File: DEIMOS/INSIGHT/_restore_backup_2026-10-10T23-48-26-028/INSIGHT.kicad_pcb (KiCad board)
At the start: 4 copper layers, 69.9 x 26 mm, 79 parts, among them J1 Batt, J3 USB_C_Receptacle_USB2.0_16P, J4 Boot, J5 GND, J8 5V, SW3 SW_SPDT, U1 LSM6DS3, U11 MPM3610GQV-Z, U2 MPL3115A2, U3 W25Q128JVSIQ, U5 RP2040, U6 Adafruit GPS, U7 MPM3610GQV-Z, Y1 ABM8-272-T3

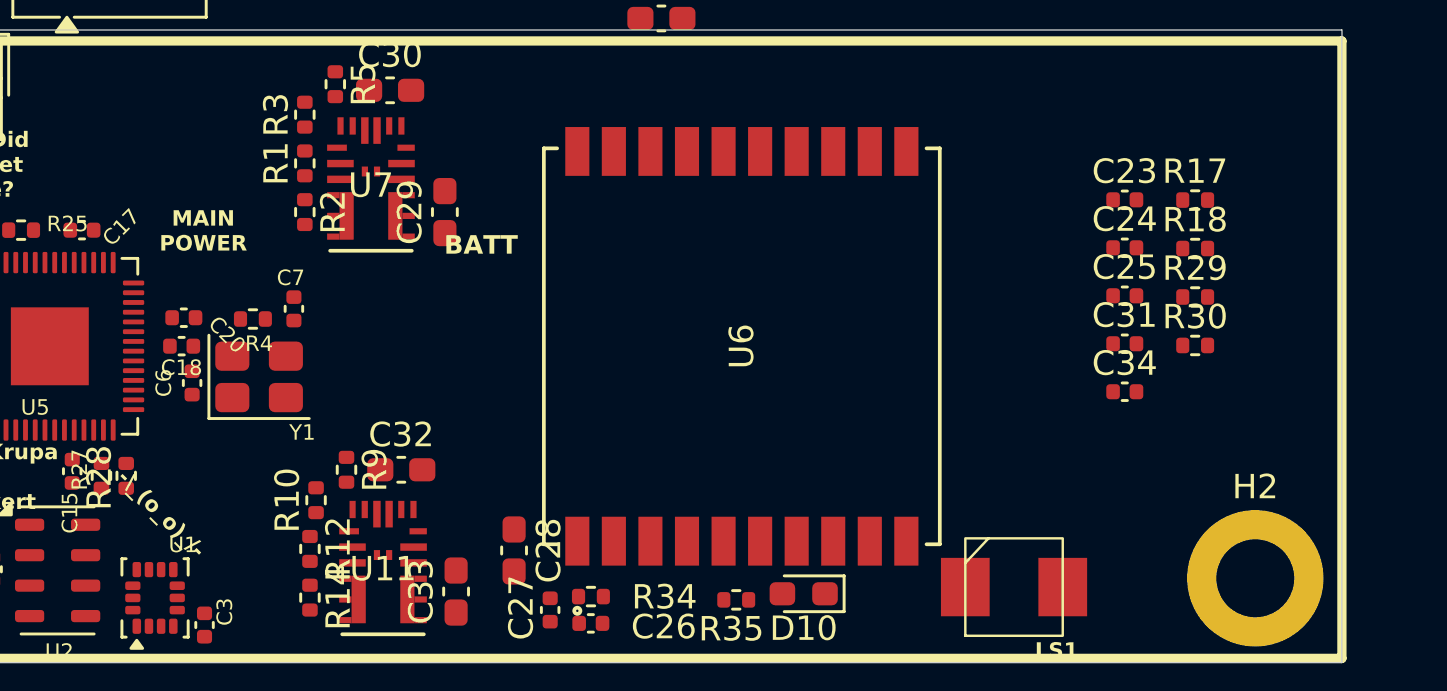
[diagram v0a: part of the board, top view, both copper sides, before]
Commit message: Updated Insight schemtic to use rfm95W
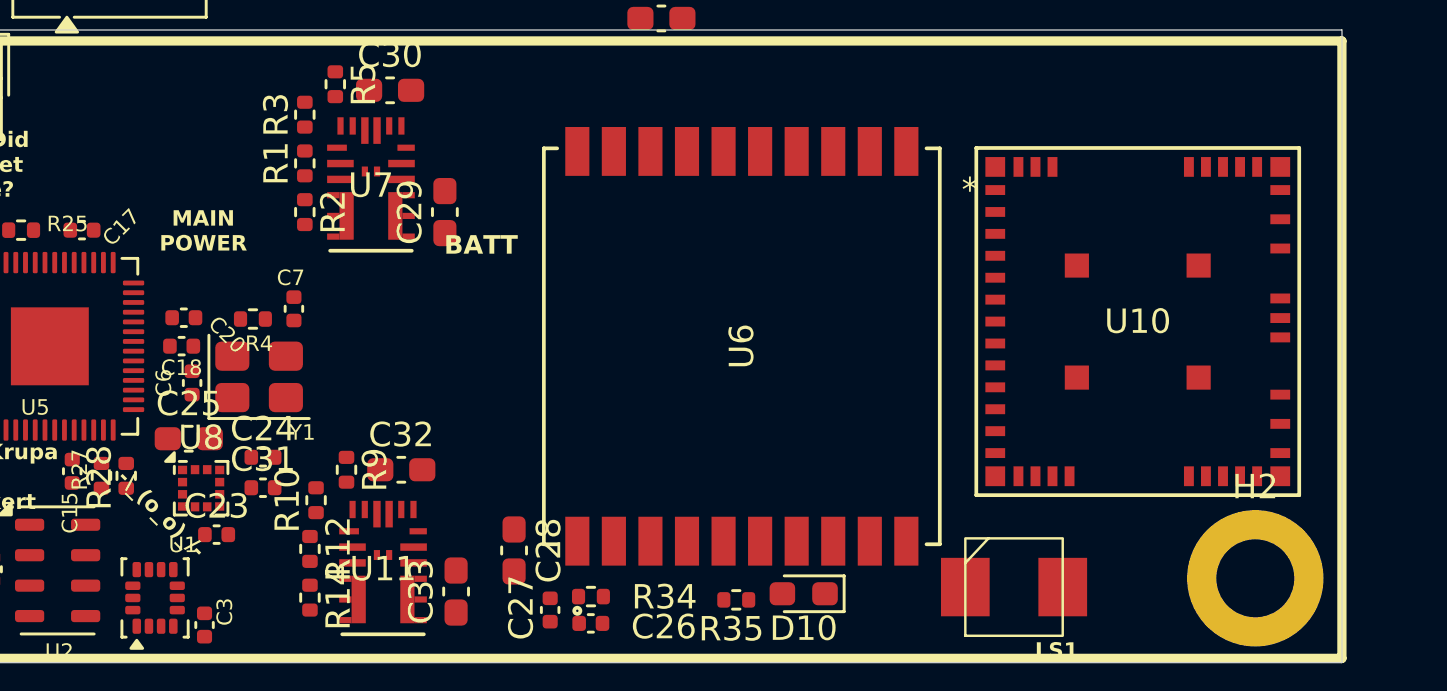
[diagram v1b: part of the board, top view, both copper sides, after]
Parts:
- removed C34: 22p, Capacitor_SMD:C_0402_1005Metric
- removed R17, R18: 10k, Resistor_SMD:R_0402_1005Metric
- removed R29, R30: 4.7k, Resistor_SMD:R_0402_1005Metric
- added U10: 453-00139R, 453_00140R:MOD47_RM126x_LRD, F.Cu at (128.8, 72.4)
- added U8: IIS2MDCTR, Package_LGA:LGA-12_2x2mm_P0.5mm, F.Cu at (90.3, 79.2)
- C25: value 100n -> 10u; footprint Capacitor_SMD:C_0402_1005Metric -> Capacitor_SMD:C_0603_1608Metric_Pad1.08x0.95mm_HandSolder
- C31: value 22p -> 100n
- moved C23 39.7 mm to (91.0, 81.1)
- moved C25 38.9 mm to (89.8, 77.2)
- moved C24 36.4 mm to (92.9, 78.0)
- moved C31 35.9 mm to (92.9, 79.2)
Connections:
- net /H_INTN renamed /Card Detect
- C23 pad 1: +3V3 -> Net-(U8-C1)
- C25 pad 1: Net-(U4-CAP) -> +3V3
- C31 pad 1: Net-(U4-XOUT32/CLKSEL1) -> +3V3
- U5 pad 9: /NRST -> /GPIO7
